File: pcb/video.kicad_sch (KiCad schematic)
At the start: 5 parts

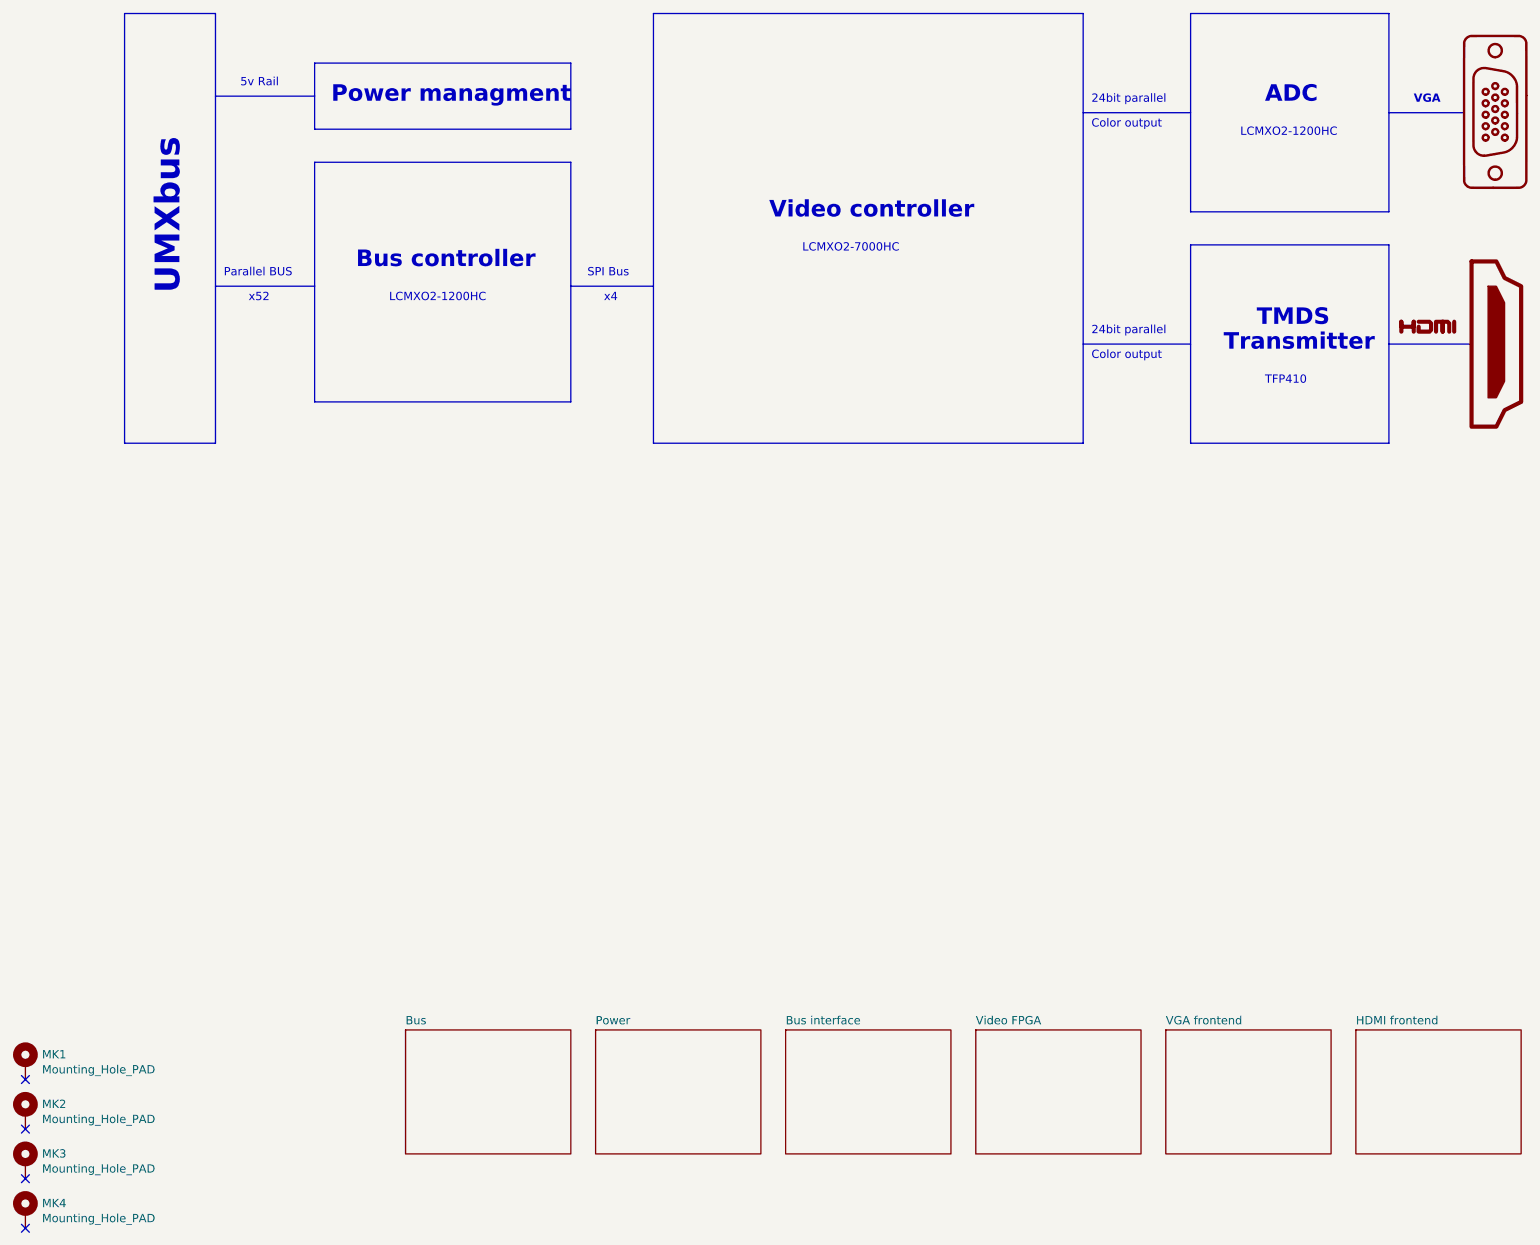
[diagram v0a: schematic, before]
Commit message: add jtag and spi tag connect to the bus fpga
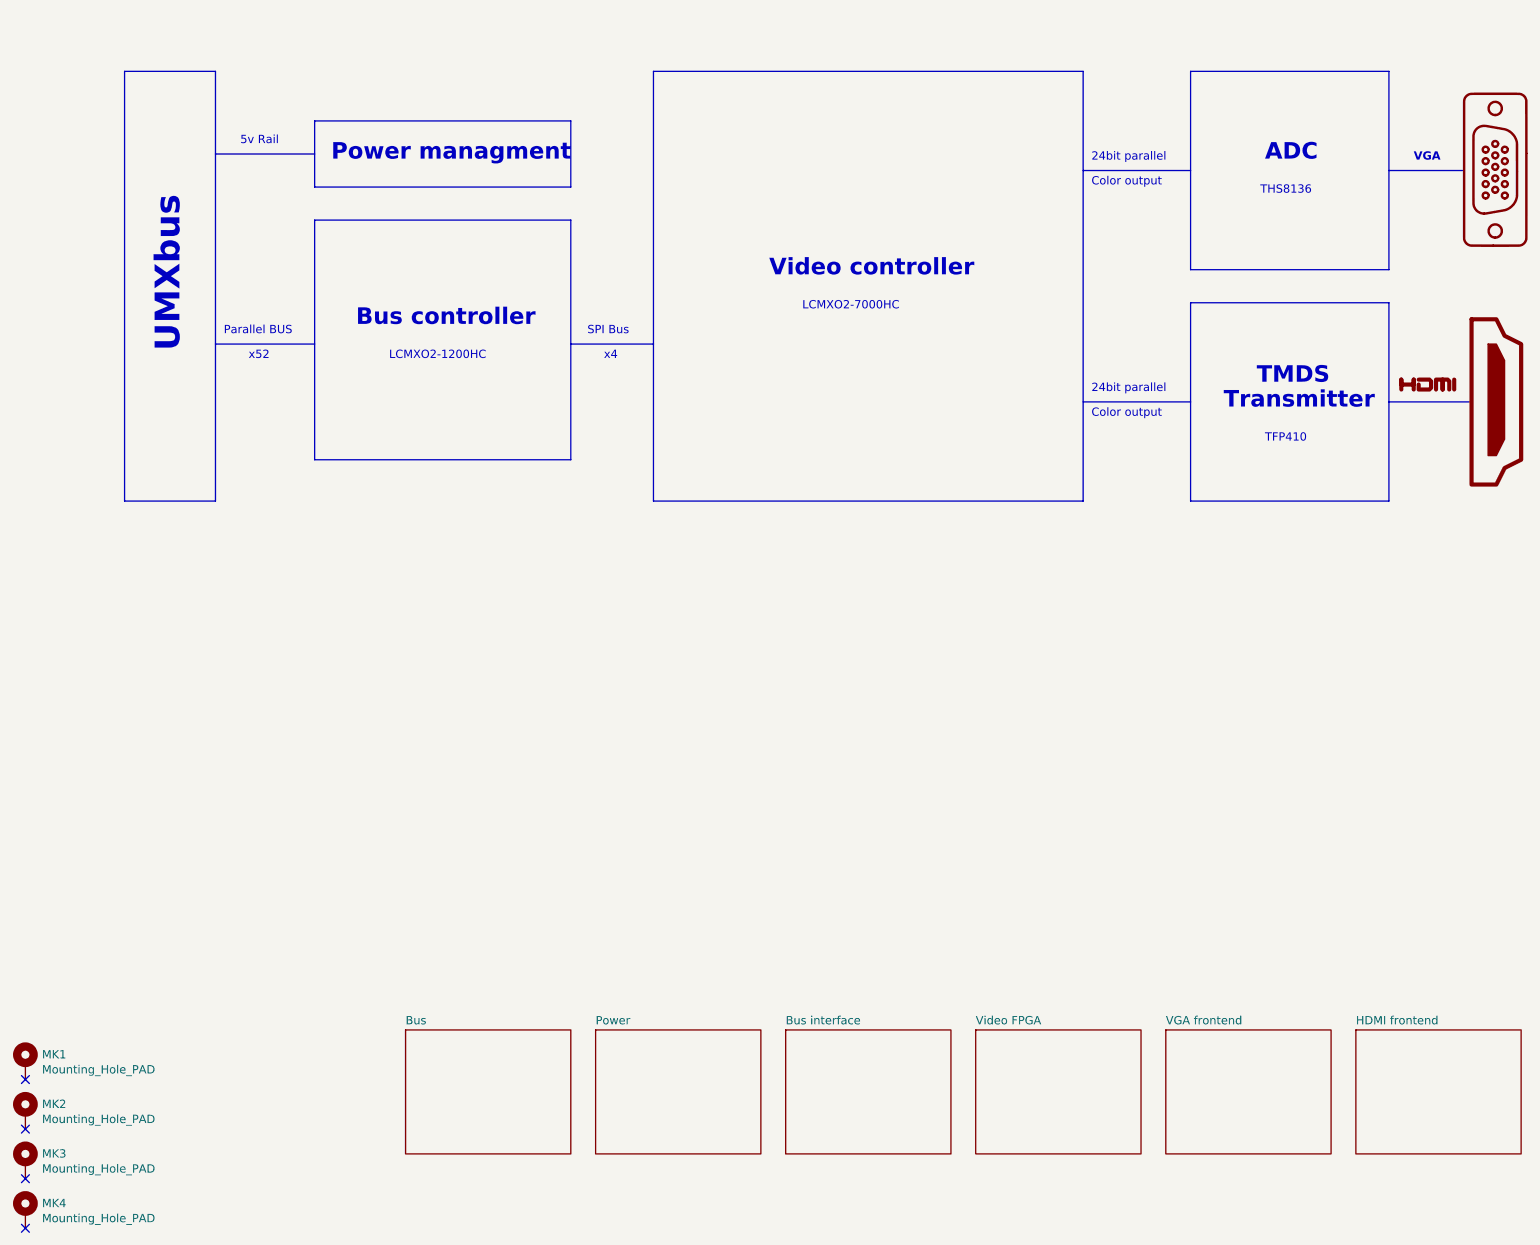
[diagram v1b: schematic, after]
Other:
- note added: "THS8136"
- title: (none) -> Video card overview

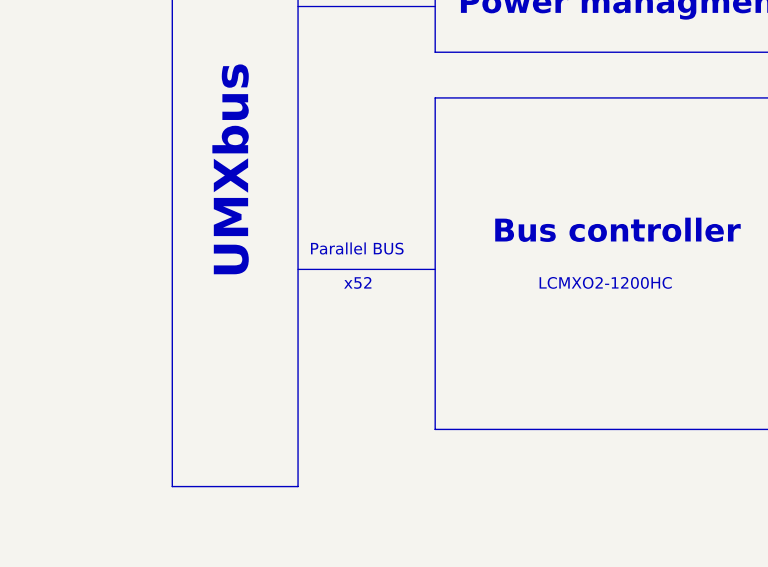
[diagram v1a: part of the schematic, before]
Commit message: add connector labels
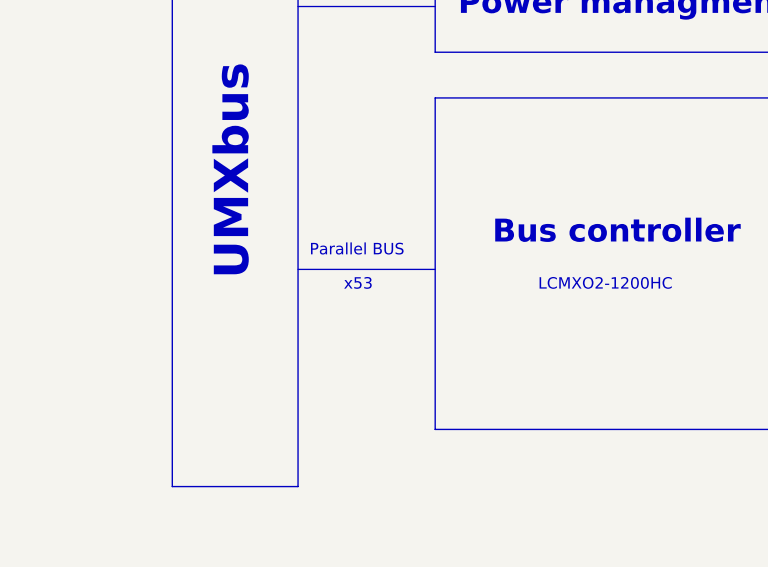
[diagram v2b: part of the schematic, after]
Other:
- note added: "x53"
- note removed: "x52"
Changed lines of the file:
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@@
     (effects (font (size 1.27 1.27)) (justify left bottom))
   )
-  (text "x52" (at 58.42 115.57 0)
+  (text "x53" (at 58.42 115.57 0)
     (effects (font (size 1.27 1.27)) (justify left bottom))
   )

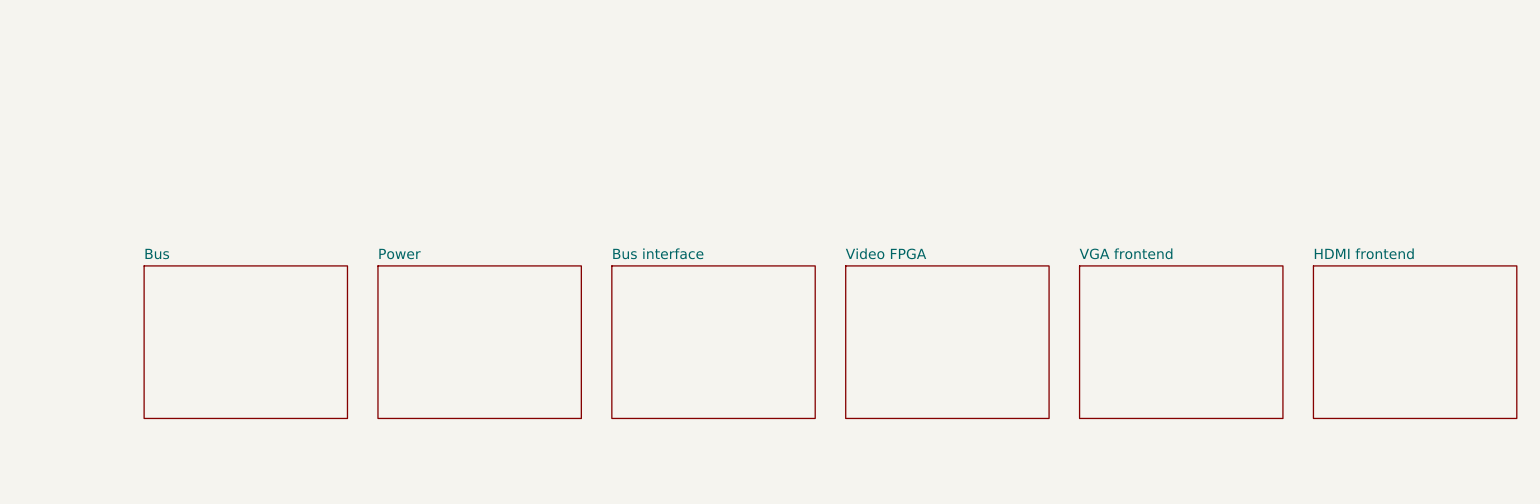
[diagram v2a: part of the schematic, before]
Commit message: add bypass to the video controller
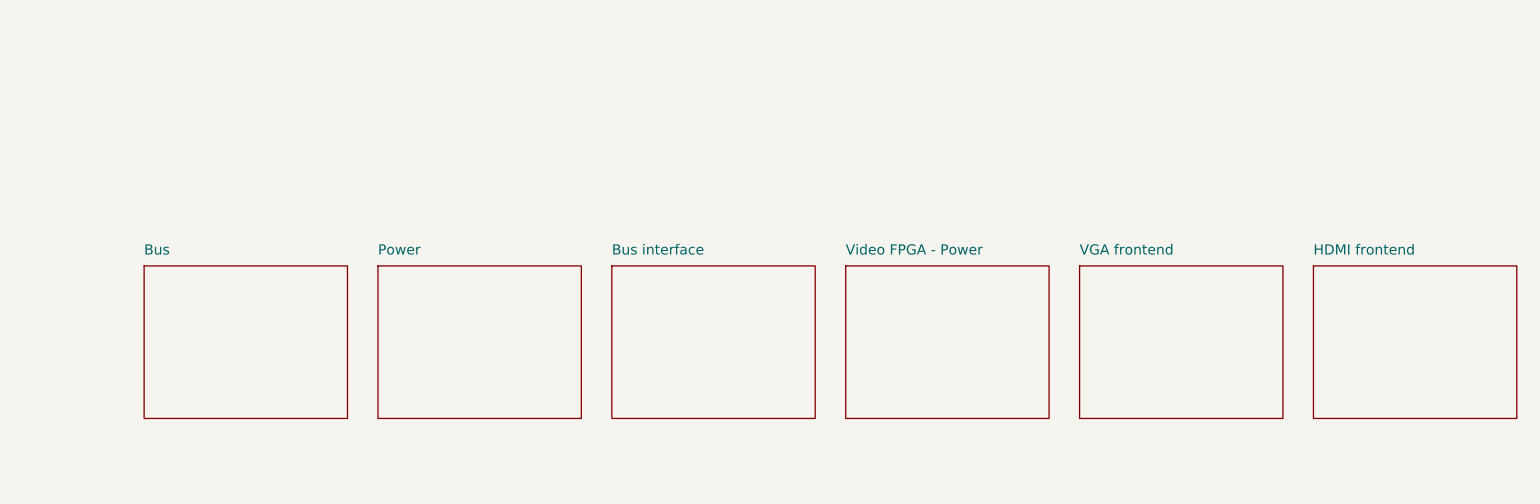
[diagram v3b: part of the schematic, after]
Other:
- sheet Bus interface renamed Bus interface 
- sheet Video FPGA renamed Video FPGA - Power
